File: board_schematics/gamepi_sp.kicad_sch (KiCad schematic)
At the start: 9 parts, among them SW1 SW_Push

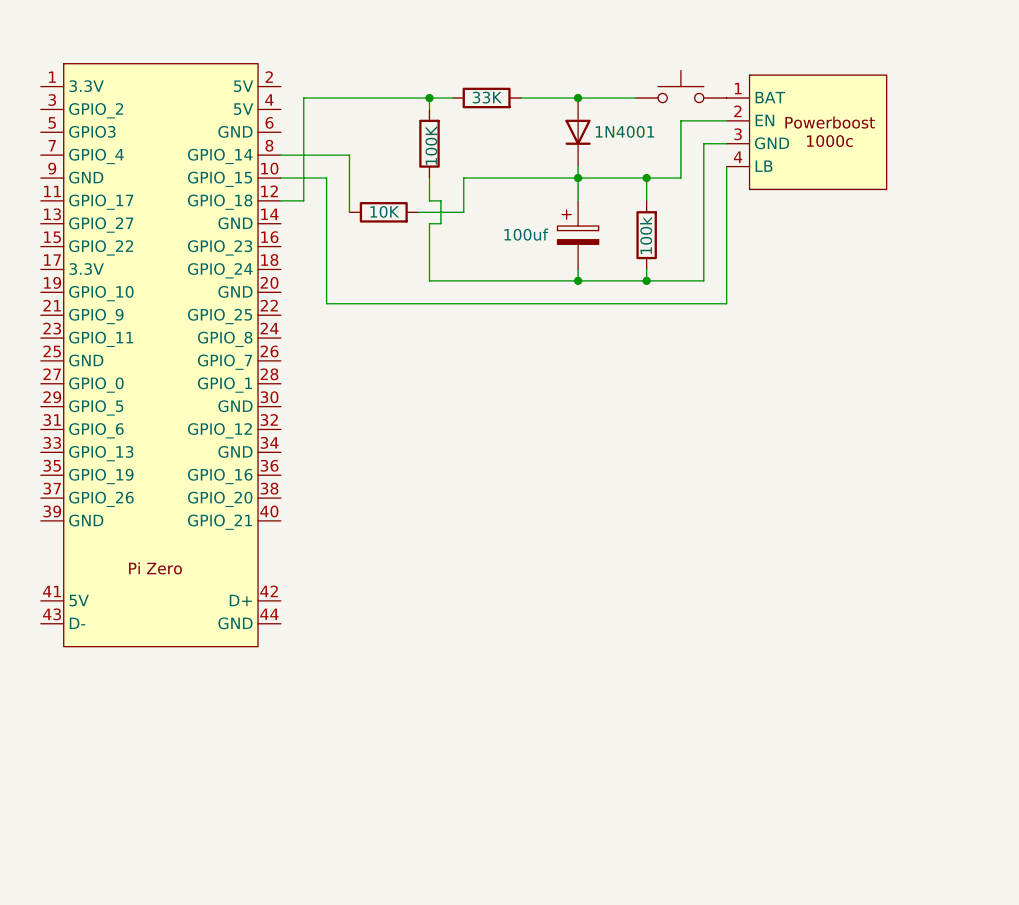
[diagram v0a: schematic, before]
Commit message: added controler buttons to schematic
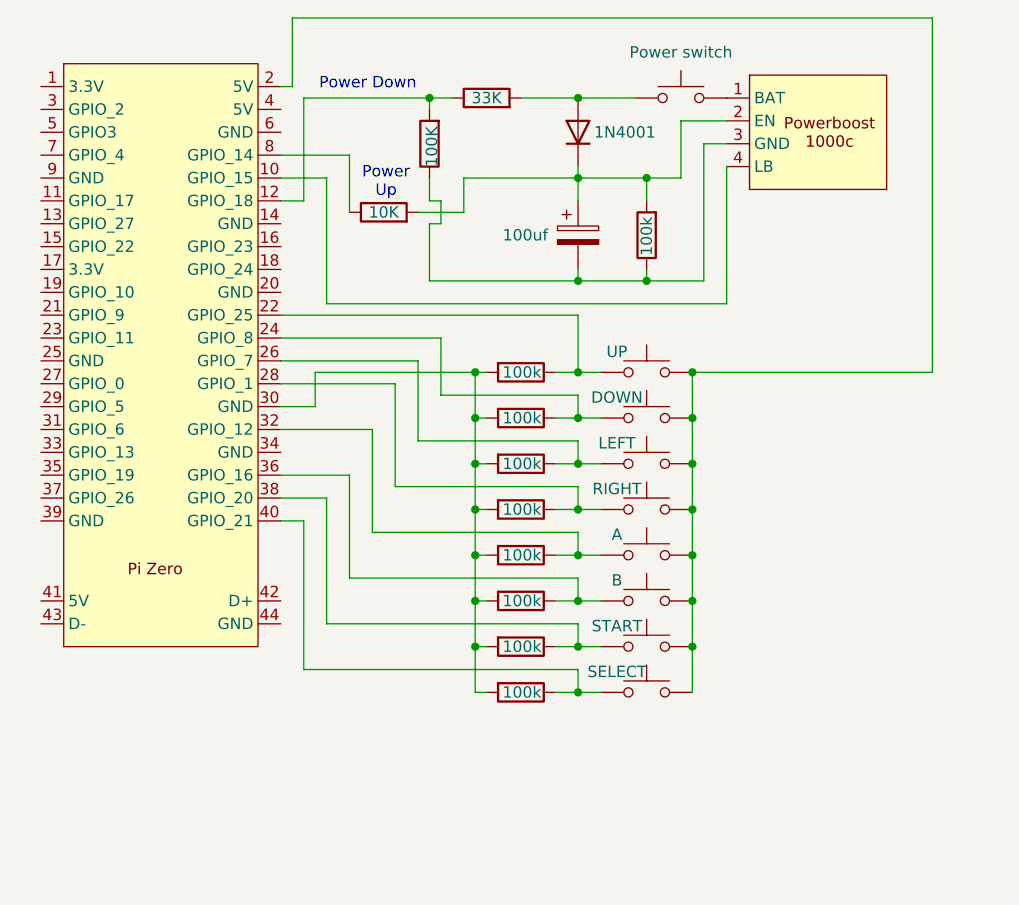
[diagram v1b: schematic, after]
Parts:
- added R10, R11, R12, R5, R6, R7, R8, R9: 100k, Resistor_SMD:R_0201_0603Metric, symbol Device:R
- added SW2: UP, Button_Switch_THT:SW_PUSH_6mm, symbol Switch:SW_Push
- added SW3: DOWN, Button_Switch_THT:SW_PUSH_6mm, symbol Switch:SW_Push
- added SW4: LEFT, Button_Switch_THT:SW_PUSH_6mm, symbol Switch:SW_Push
- added SW5: RIGHT, Button_Switch_THT:SW_PUSH_6mm, symbol Switch:SW_Push
- added SW6: A, Button_Switch_THT:SW_PUSH_6mm, symbol Switch:SW_Push
- added SW7: B, Button_Switch_THT:SW_PUSH_6mm, symbol Switch:SW_Push
- added SW8: START, Button_Switch_THT:SW_PUSH_6mm, symbol Switch:SW_Push
- added SW9: SELECT, Button_Switch_THT:SW_PUSH_6mm, symbol Switch:SW_Push
- SW1: value SW_Push -> Power switch
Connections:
- net at U1.2 (5V): now also SW2.2, SW3.2, SW4.2, SW5.2, SW6.2, SW7.2, SW8.2, SW9.2
- net at U1.22 (GPIO_25): now also R12.1, SW2.1
- net at U1.24 (GPIO_8): now also R7.1, SW3.1
- net at U1.26 (GPIO_7): now also R6.1, SW4.1
- net at U1.28 (GPIO_1): now also R5.1, SW5.1
- net at U1.30 (GND): now also R10.2, R11.2, R12.2, R5.2, R6.2, R7.2, R8.2, R9.2
- net at U1.32 (GPIO_12): now also R11.1, SW6.1
- net at U1.36 (GPIO_16): now also R10.1, SW7.1
- net at U1.38 (GPIO_20): now also R9.1, SW8.1
- net at U1.40 (GPIO_21): now also R8.1, SW9.1
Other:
- note added: "Power Down"
- note added: "Power Up"

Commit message: started documentation for assesment
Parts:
- added R13, R14: 100k, Resistor_SMD:R_0201_0603Metric, symbol Device:R
- added SW10: R, Button_Switch_THT:SW_PUSH_6mm, symbol Switch:SW_Push
- added SW11: L, Button_Switch_THT:SW_PUSH_6mm, symbol Switch:SW_Push
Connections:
- net at R5.1, SW5.1: now also U1.24 (GPIO_8); no longer U1.28 (GPIO_1)
- net at SW2.2, SW3.2, SW4.2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: now also SW10.2, SW11.2
- net at R6.1, SW4.1: now also U1.22 (GPIO_25); no longer U1.26 (GPIO_7)
- net at R7.1, SW3.1: now also U1.18 (GPIO_24); no longer U1.24 (GPIO_8)
- net at R8.1, SW9.1: now also U1.36 (GPIO_16); no longer U1.40 (GPIO_21)
- net at R10.2, R11.2, R12.2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: now also R13.2, R14.2
- net at R10.1, SW7.1: now also U1.28 (GPIO_1); no longer U1.36 (GPIO_16)
- net at R9.1, SW8.1: now also U1.32 (GPIO_12); no longer U1.38 (GPIO_20)
- net at R12.1, SW2.1: now also U1.16 (GPIO_23); no longer U1.22 (GPIO_25)
- net at R11.1, SW6.1: now also U1.26 (GPIO_7); no longer U1.32 (GPIO_12)
- new net: R13.1, SW10.1, U1.38 (GPIO_20)
- new net: R14.1, SW11.1, U1.40 (GPIO_21)

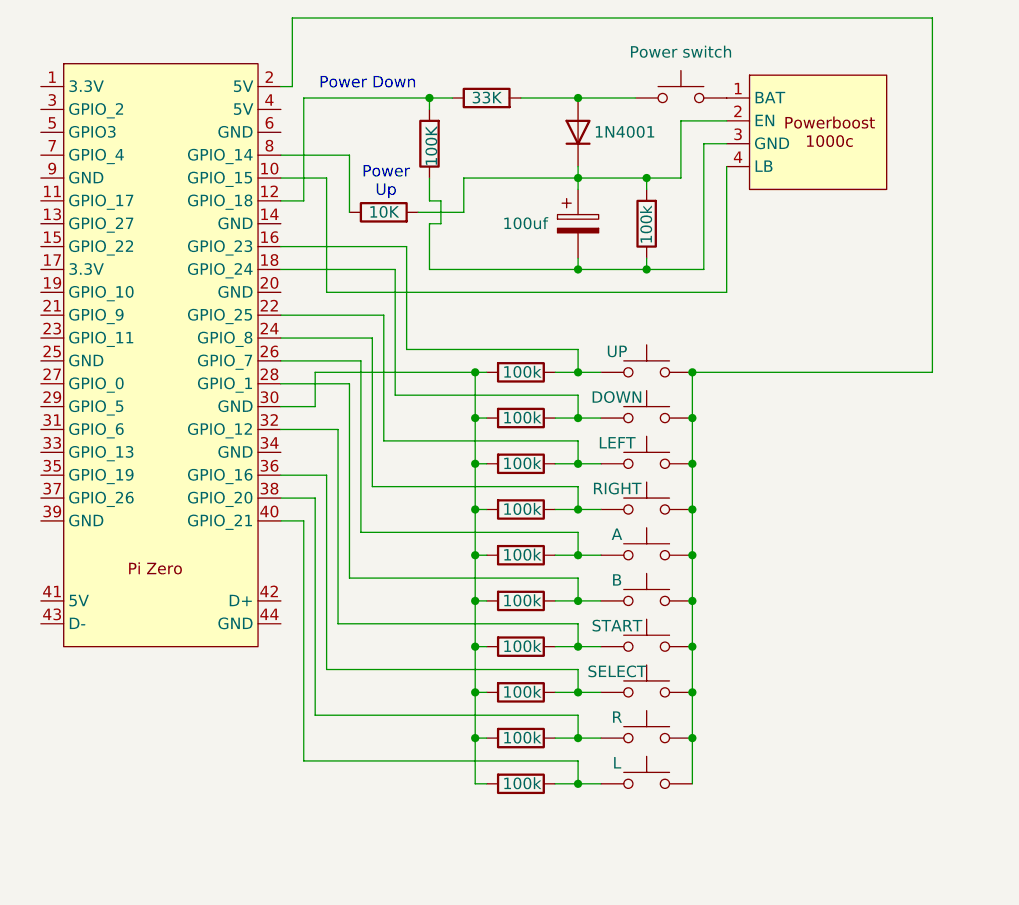
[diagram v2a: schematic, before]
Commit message: changed schematic from push button to slideswitch layout
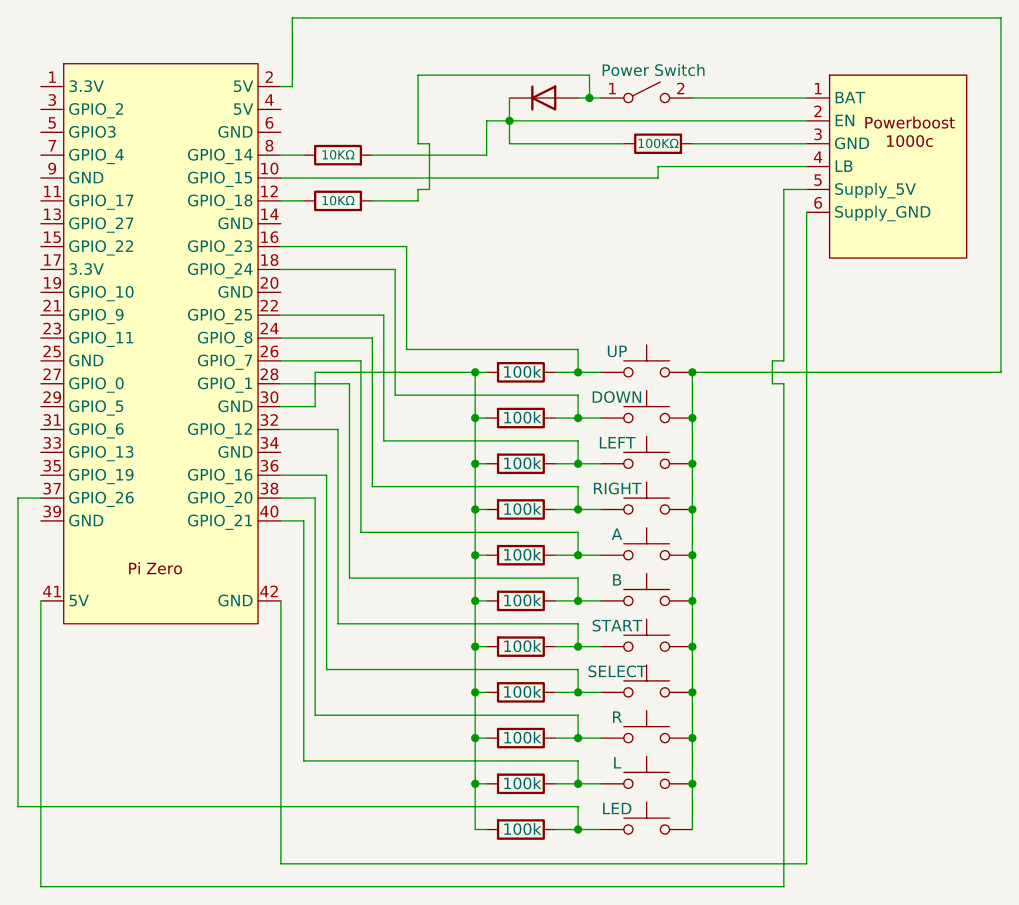
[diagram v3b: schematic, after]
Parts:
- removed C1: 100uf, symbol Device:C_Polarized
- added SW12: Power Switch, Button_Switch_THT:SW_E-Switch_EG1271_SPDT, symbol Switch:SW_DPST_x2
- D1: value 1N4001 -> D; footprint (none) -> Resistor_SMD:R_0201_0603Metric
- R1: value 33K -> 100KΩ
- R2: value 100K -> 10KΩ
- R3: value 10K -> 10KΩ
- SW1: value Power switch -> LED
- U1: footprint (none) -> gamepi_sp:pi_zero_pcb_pins
- U2: footprint (none) -> gamepi_sp:powerboost_1000C_pins
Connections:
- net at SW10.2, SW11.2, SW2.2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: now also SW1.2
- net at U2.1 (BAT): now also SW12.2 (B); no longer SW1.2
- net at D1.1 (K), U2.2 (EN): now also R1.1, R2.2; no longer R3.2, R4.2
- net at R10.2, R11.2, R12.2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: now also R4.2
- net at R3.1: now also U1.12 (GPIO_18); no longer U1.8 (GPIO_14)
- net at U1.37 (GPIO_26): now also R4.1, SW1.1
- net at U1.41 (5V): now also U2.5 (Supply_5V)
- net at U1.42 (GND): now also U2.6 (Supply_GND)
- new net: D1.2 (A), R3.2, SW12.1 (A)
- new net: R2.1, U1.8 (GPIO_14)
- new net: R1.2, U2.3 (GND)
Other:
- note removed: "Power Down"
- note removed: "Power Up"

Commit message: pcb design is hard :c
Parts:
- D1, R1, R10, R11, R12, R13, R14, R2, R3, R4, R5, R6, R7, R8, R9: footprint Resistor_SMD:R_0201_0603Metric -> Resistor_THT:R_Axial_DIN0204_L3.6mm_D1.6mm_P5.08mm_Horizontal
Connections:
- net at SW5.1, U1.24 (GPIO_8): now also R6.1; no longer R5.1
- net at SW4.1, U1.22 (GPIO_25): now also R5.1; no longer R6.1
- net at SW3.1, U1.18 (GPIO_24): now also R4.1; no longer R7.1
- net at SW9.1, U1.36 (GPIO_16): now also R10.1; no longer R8.1
- net at SW10.1, U1.38 (GPIO_20): now also R11.1; no longer R13.1
- net at SW7.1, U1.28 (GPIO_1): now also R8.1; no longer R10.1
- net at SW6.1, U1.26 (GPIO_7): now also R7.1; no longer R11.1
- net at SW1.1, U1.37 (GPIO_26): now also R14.1; no longer R4.1
- net at SW11.1, U1.40 (GPIO_21): now also R13.1; no longer R14.1
